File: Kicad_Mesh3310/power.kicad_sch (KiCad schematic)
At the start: 19 parts, among them J9 Battery, SW18 POWER ON/OFF, U1 MAX1555, U14 TPS63031DSK, U9 MAX16054

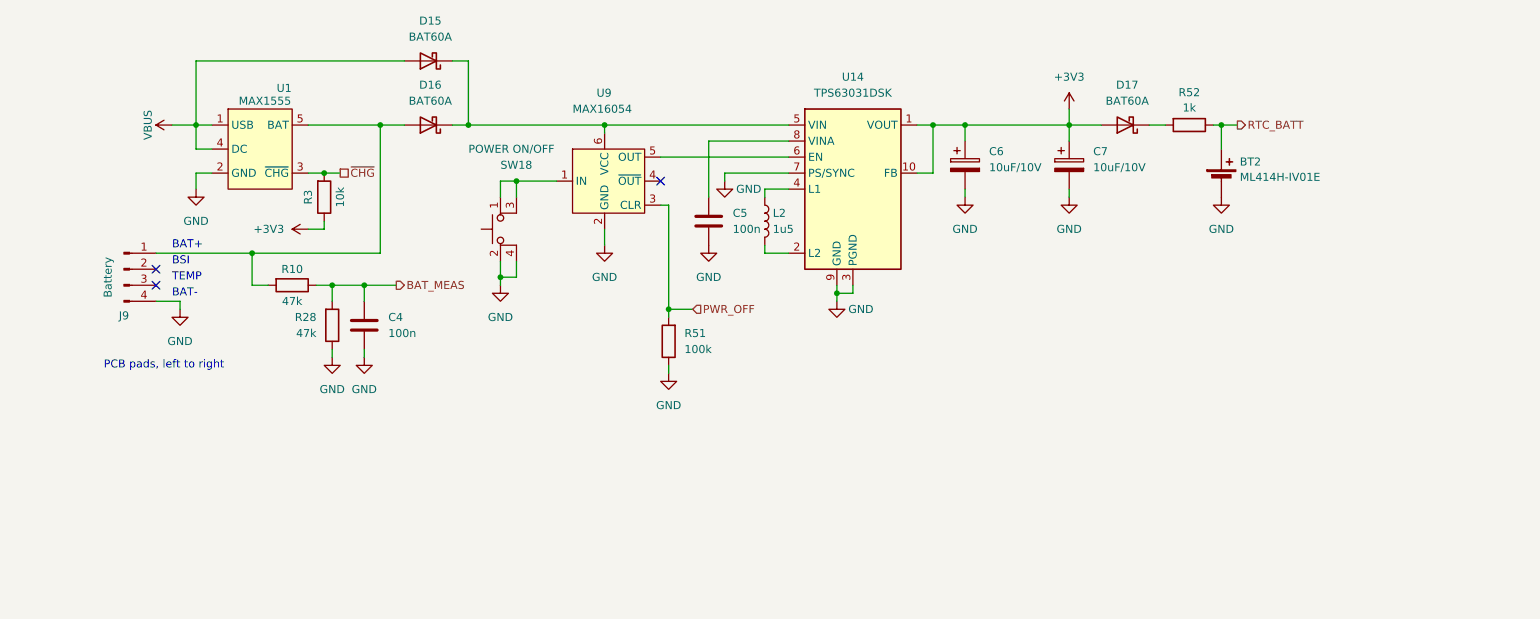
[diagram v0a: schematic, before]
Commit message: Battery ic changes
form Max1555 to BQ24074
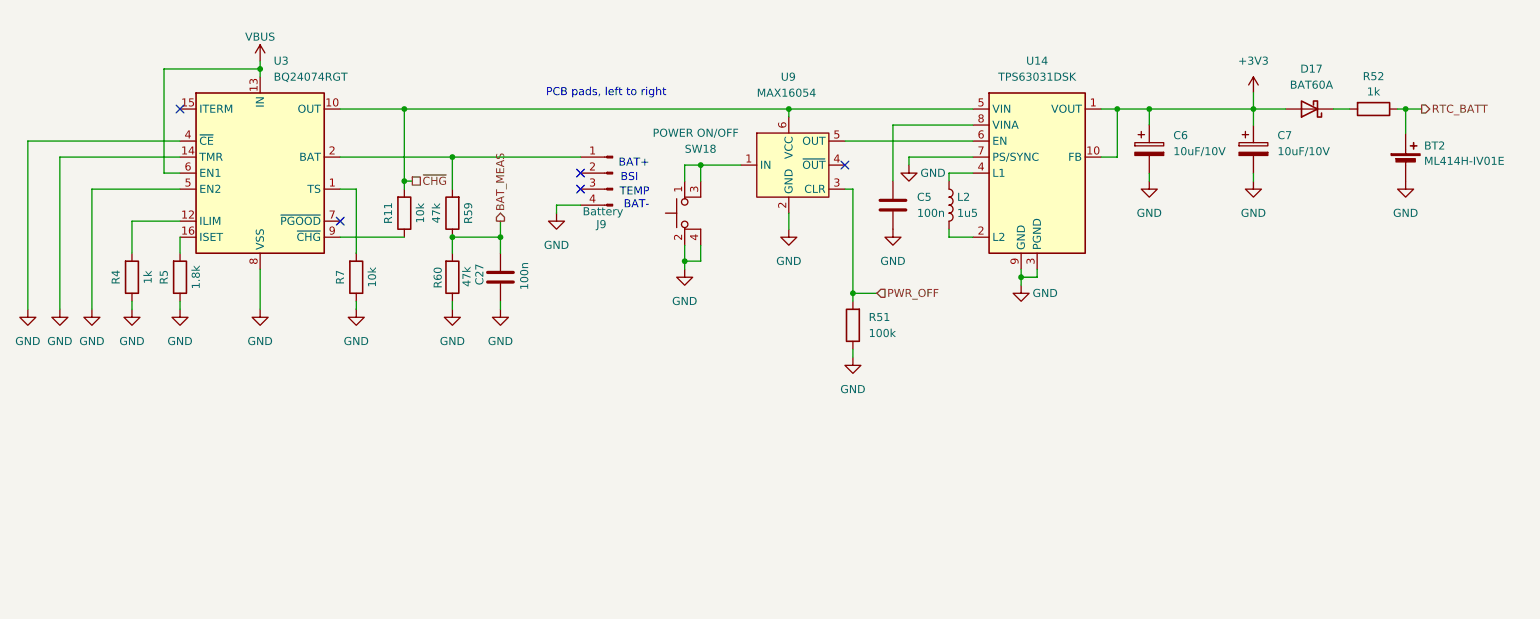
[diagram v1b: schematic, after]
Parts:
- removed C4: 100n, Capacitor_SMD:C_0402_1005Metric, symbol Device:C
- removed D15, D16: BAT60A, Diode_SMD:D_SOD-323, symbol Diode:BAT60A
- removed R10, R28: 47k, Resistor_SMD:R_0402_1005Metric, symbol Device:R
- removed R3: 10k, Resistor_SMD:R_0402_1005Metric, symbol Device:R
- removed U1: MAX1555, Package_TO_SOT_SMD:TSOT-23-5, symbol Parts:MAX1555
- added C27: 100n, Capacitor_SMD:C_0402_1005Metric, symbol Device:C
- added R11, R7: 10k, Resistor_SMD:R_0402_1005Metric, symbol Device:R
- added R4: 1k, Resistor_SMD:R_0402_1005Metric, symbol Device:R
- added R5: 1.8k, Resistor_SMD:R_0402_1005Metric, symbol Device:R
- added R59, R60: 47k, Resistor_SMD:R_0402_1005Metric, symbol Device:R
- added U3: BQ24074RGT, Package_DFN_QFN:VQFN-16-1EP_3x3mm_P0.5mm_EP1.6x1.6mm, symbol Battery_Management:BQ24074RGT
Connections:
- net BAT_MEAS: now also C27.2, R59.1, R60.2
- net GND: now also C27.1, R4.1, R5.1, R60.1, R7.1, U3.14 (TMR), U3.17 (VSS), U3.4 (~{CE}), U3.5 (EN2), U3.8 (VSS)
- net VBUS: now also U3.13 (IN), U3.6 (EN1)
- net ~{CHG}: now also U14.5 (VIN), U9.6 (VCC), R11.2, U3.10 (OUT), U3.11 (OUT)
- net at J9.1 (Pin_1): now also R59.2, U3.2 (BAT), U3.3 (BAT)
- new net: R4.2, U3.12 (ILIM)
- new net: R11.1, U3.9 (~{CHG})
- new net: R7.2, U3.1 (TS)
- new net: R5.2, U3.16 (ISET)
- no-connect marks 3 -> 5
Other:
- moved on the sheet: BT2, C5, C6, C7, D17, J9, L2, R51, R52, SW18, U14, U9

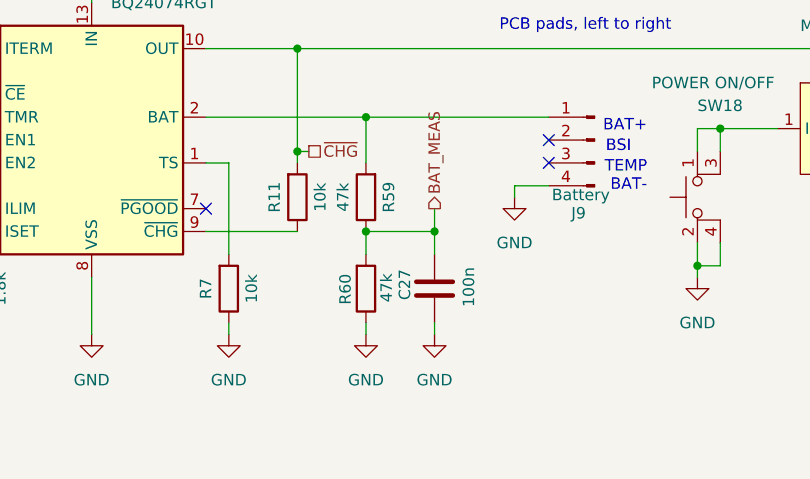
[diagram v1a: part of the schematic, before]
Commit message: Cleaning and placing
Cleaning and placing components
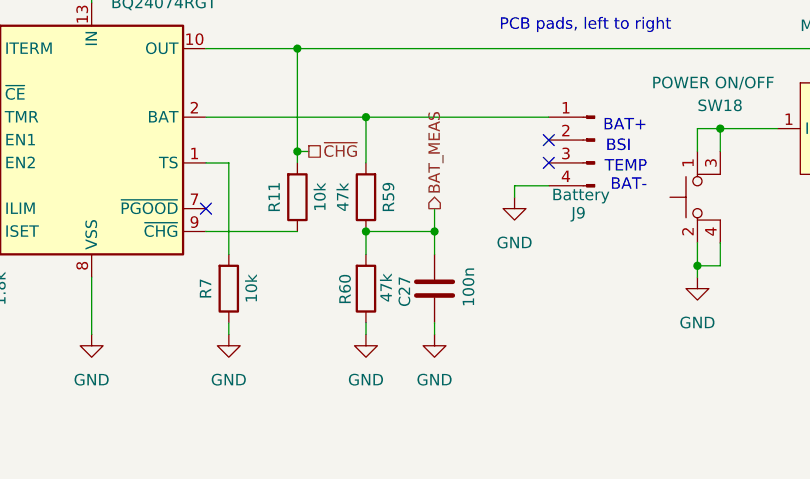
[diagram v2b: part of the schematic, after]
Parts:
- BT2: footprint Parts:ML414H -> mesh3310_footprints:ML414H
- J9: footprint Parts:3310_batt -> mesh3310_footprints:3310_batt
- SW18: footprint Parts:SIDE PUSH 2.2NF 4.7x3.2x1.65mm -> mesh3310_footprints:SIDE PUSH 2.2NF 4.7x3.2x1.65mm
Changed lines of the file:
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@@
 			)
 		)
-		(property "Footprint" "Parts:ML414H"
+		(property "Footprint" "mesh3310_footprints:ML414H"
 			(at 256.54 87.376 90)
 			(effects
@@
 			)
 		)
-		(property "Footprint" "Parts:3310_batt"
+		(property "Footprint" "mesh3310_footprints:3310_batt"
 			(at 130.81 90.17 0)
 			(effects
@@
 		(dnp no)
 		(property "Reference" "C27"
-			(at 109.728 107.95 90)
+			(at 109.728 108.712 90)
 			(effects
 				(font
@@
 			)
 		)
-		(property "Footprint" "Parts:SIDE PUSH 2.2NF 4.7x3.2x1.65mm"
+		(property "Footprint" "mesh3310_footprints:SIDE PUSH 2.2NF 4.7x3.2x1.65mm"
 			(at 137.16 96.52 0)
 			(effects

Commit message: RF designing
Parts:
- C6, C7: footprint Capacitor_Tantalum_SMD:CP_EIA-3528-21_Kemet-B -> Capacitor_Tantalum_SMD:CP_EIA-1608-08_AVX-J
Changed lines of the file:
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@@
 			)
 		)
-		(property "Footprint" "Capacitor_Tantalum_SMD:CP_EIA-3528-21_Kemet-B"
+		(property "Footprint" "Capacitor_Tantalum_SMD:CP_EIA-1608-08_AVX-J"
 			(at 233.3752 90.17 0)
 			(effects
@@
 			)
 		)
-		(property "Footprint" "Capacitor_Tantalum_SMD:CP_EIA-3528-21_Kemet-B"
+		(property "Footprint" "Capacitor_Tantalum_SMD:CP_EIA-1608-08_AVX-J"
 			(at 216.8652 90.17 0)
 			(effects

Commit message: Lora antenna replacement
Lora antenna replacement, added Nordic nRF 9151 for GPS , VoIP ,VoLTE-m , SIP
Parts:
- C27, C5: footprint Capacitor_SMD:C_0402_1005Metric -> Capacitor_SMD:C_0201_0603Metric
- R11, R4, R5, R51, R52, R59, R60, R7: footprint Resistor_SMD:R_0402_1005Metric -> Resistor_SMD:R_0201_0603Metric
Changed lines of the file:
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@@
 			)
 		)
-		(property "Footprint" "Resistor_SMD:R_0402_1005Metric"
+		(property "Footprint" "Resistor_SMD:R_0201_0603Metric"
 			(at 103.632 106.68 90)
 			(effects
@@
 			)
 		)
-		(property "Footprint" "Resistor_SMD:R_0402_1005Metric"
+		(property "Footprint" "Resistor_SMD:R_0201_0603Metric"
 			(at 170.688 114.3 90)
 			(effects
@@
 			)
 		)
-		(property "Footprint" "Resistor_SMD:R_0402_1005Metric"
+		(property "Footprint" "Resistor_SMD:R_0201_0603Metric"
 			(at 52.832 106.68 90)
 			(effects
@@
 			)
 		)
-		(property "Footprint" "Resistor_SMD:R_0402_1005Metric"
+		(property "Footprint" "Resistor_SMD:R_0201_0603Metric"
 			(at 96.012 96.52 90)
 			(effects
@@
 			)
 		)
-		(property "Footprint" "Resistor_SMD:R_0402_1005Metric"
+		(property "Footprint" "Resistor_SMD:R_0201_0603Metric"
 			(at 107.188 96.52 90)
 			(effects
@@
 			)
 		)
-		(property "Footprint" "Capacitor_SMD:C_0402_1005Metric"
+		(property "Footprint" "Capacitor_SMD:C_0201_0603Metric"
 			(at 174.2948 91.44 0)
 			(effects
@@
 			)
 		)
-		(property "Footprint" "Resistor_SMD:R_0402_1005Metric"
+		(property "Footprint" "Resistor_SMD:R_0201_0603Metric"
 			(at 88.392 106.68 90)
 			(effects
@@
 			)
 		)
-		(property "Footprint" "Resistor_SMD:R_0402_1005Metric"
+		(property "Footprint" "Resistor_SMD:R_0201_0603Metric"
 			(at 251.46 78.232 90)
 			(effects
@@
 			)
 		)
-		(property "Footprint" "Capacitor_SMD:C_0402_1005Metric"
+		(property "Footprint" "Capacitor_SMD:C_0201_0603Metric"
 			(at 112.0648 102.87 0)
 			(effects
@@
 			)
 		)
-		(property "Footprint" "Resistor_SMD:R_0402_1005Metric"
+		(property "Footprint" "Resistor_SMD:R_0201_0603Metric"
 			(at 60.452 106.68 90)
 			(effects

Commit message: Backup work
Adding some extra pads
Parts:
- added J4: Conn_01x05_Pin, mesh3310_footprints:3310_dc, symbol Connector:Conn_01x05_Pin
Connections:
- net GND: now also J4.2 (Pin_2), J4.3 (Pin_3)
- net VBUS: now also J4.1 (Pin_1)
- new net USB_D+: J4.4 (Pin_4)
- new net USB_D-: J4.5 (Pin_5)
